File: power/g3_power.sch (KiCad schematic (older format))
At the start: 2 parts

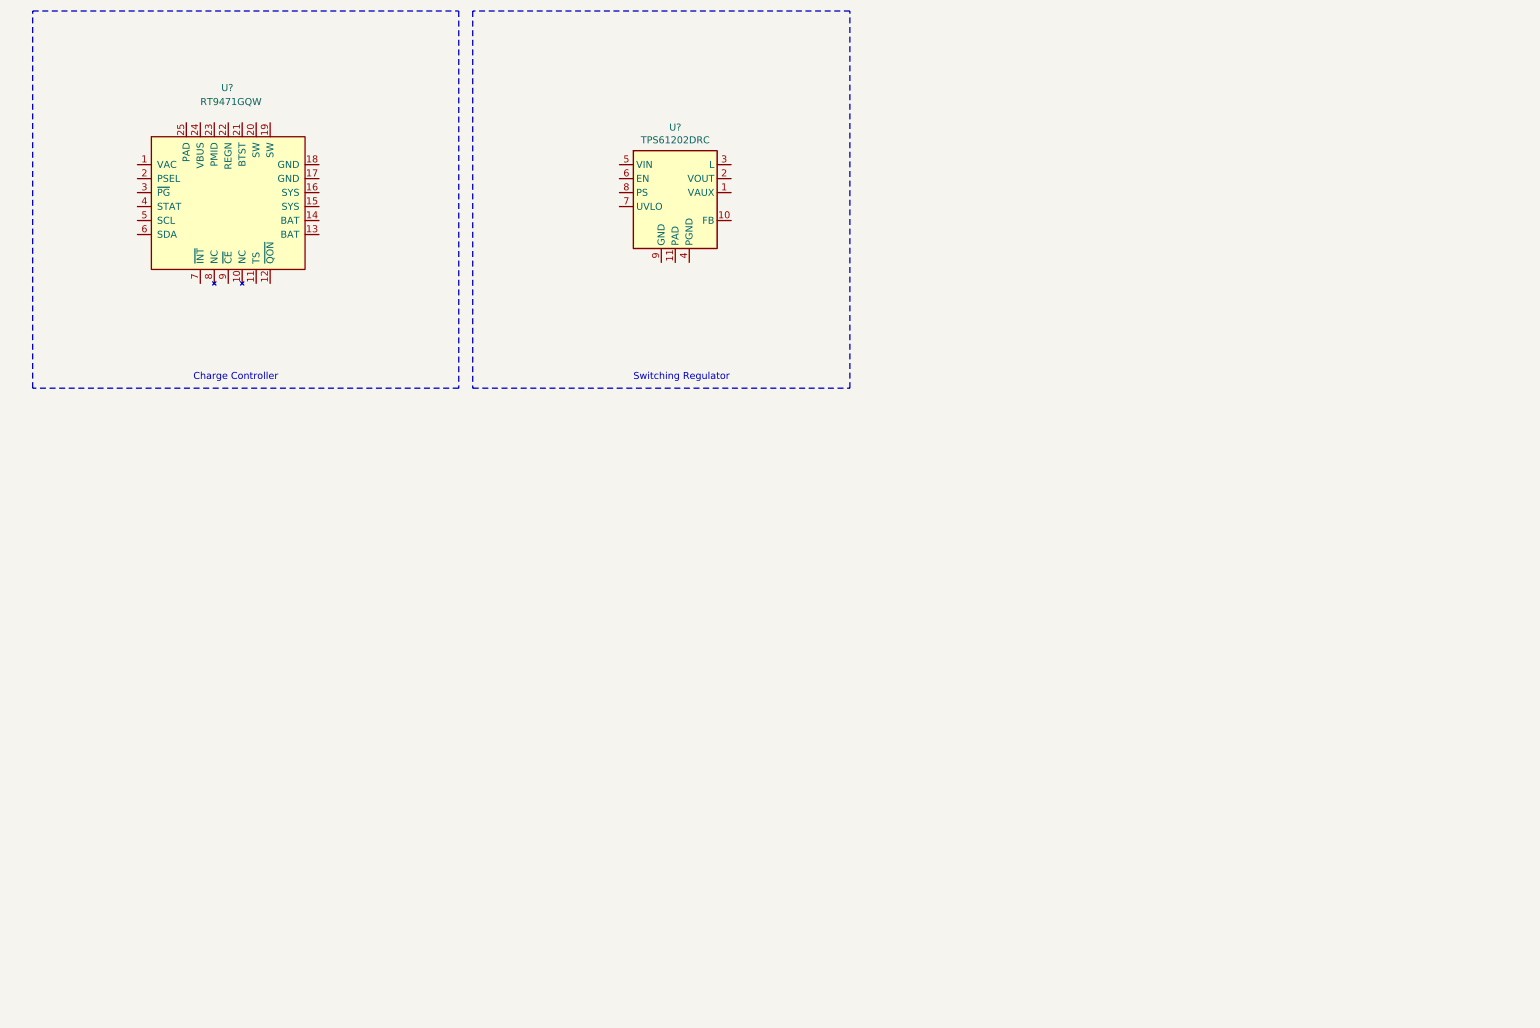
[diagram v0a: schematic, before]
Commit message: added interfacing to charge controller on schematic
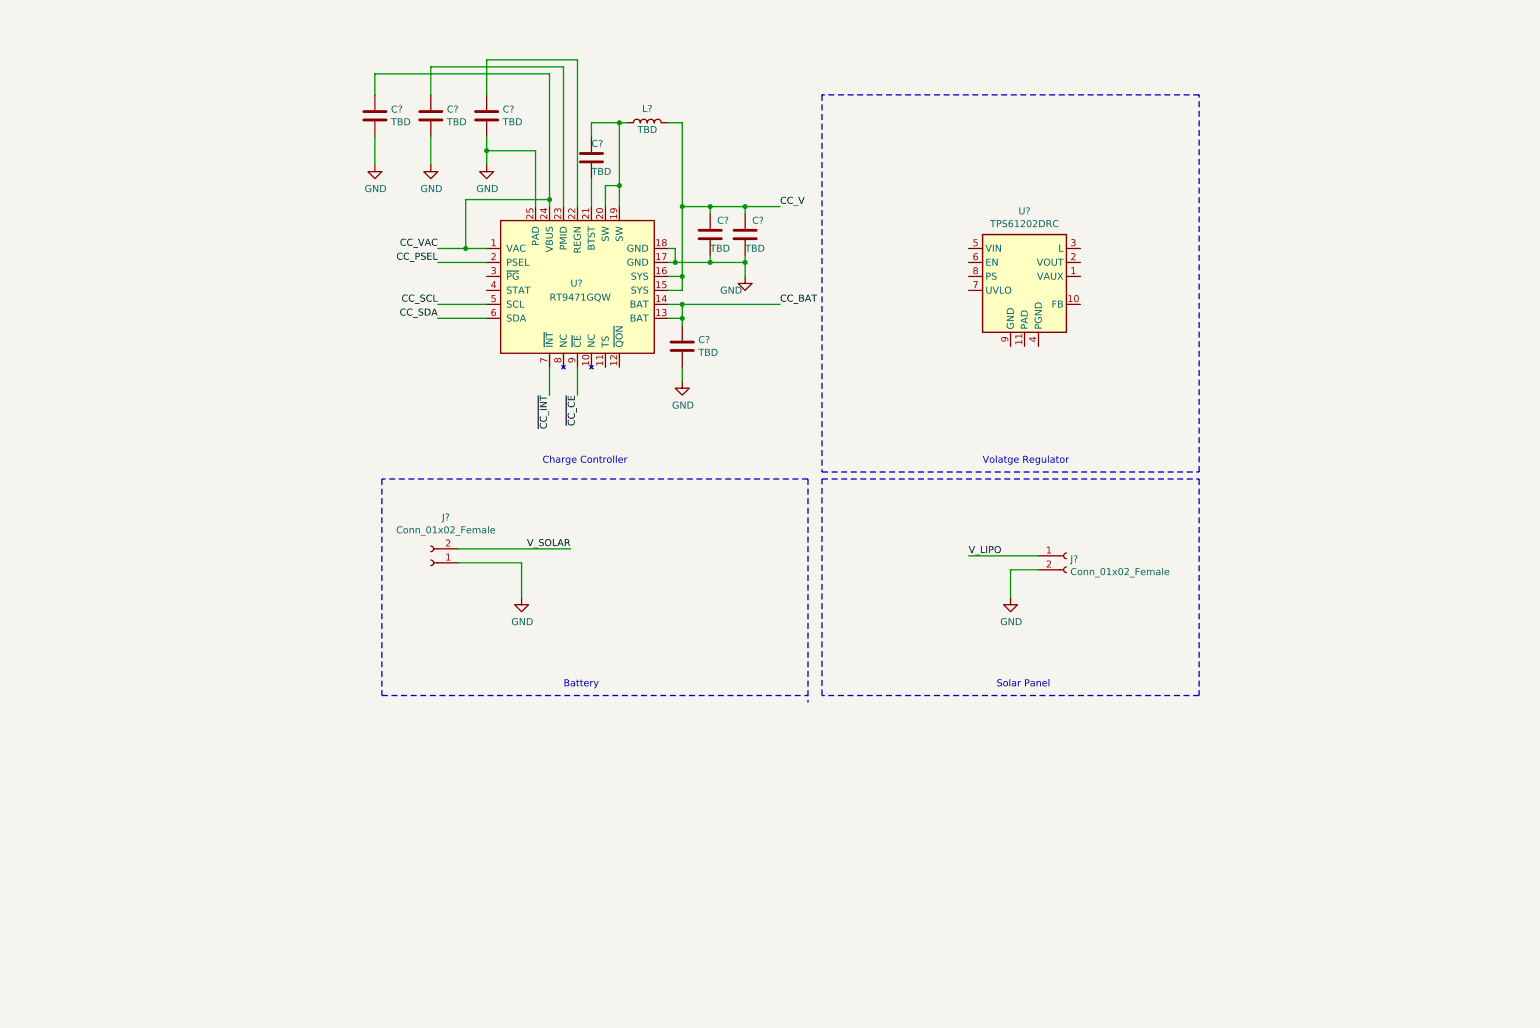
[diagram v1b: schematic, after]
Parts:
- added C? (x7): TBD, symbol Device:C
- added J? (x2): Conn_01x02_Female, symbol Connector:Conn_01x02_Female
- added L?: TBD, symbol Device:L
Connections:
- net CC_VAC: now reaches U?.1 (VAC)
- net CC_VAC: now also U?.24 (VBUS), C?.1
- net CC_BAT: now reaches U?.13 (BAT)
- net CC_BAT: now also U?.14 (BAT), C?.1
- net CC_V: now reaches U?.15 (SYS)
- net CC_V: now also U?.16 (SYS), C?.1, C?.1, L?.2
- net GND: now reaches U?.17 (GND)
- net GND: now also U?.18 (GND), U?.25 (PAD), C?.2, C?.2, C?.2, C?.2, C?.2, C?.2, J?.1 (Pin_1), J?.2 (Pin_2)
- net at U?.19 (SW): now also U?.20 (SW), C?.1, L?.1
- net CC_PSEL: now reaches U?.2 (PSEL)
- net at U?.21 (BTST): now also C?.2
- net at U?.22 (REGN): now also C?.1
- net at U?.23 (PMID): now also C?.1
- net CC_SCL: now reaches U?.5 (SCL)
- net CC_SDA: now reaches U?.6 (SDA)
- net ~CC_INT: now reaches U?.7 (~INT)
- net ~CC_CE: now reaches U?.9 (~CE)
- new net V_LIPO: J?.1 (Pin_1)
- new net V_SOLAR: J?.2 (Pin_2)
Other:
- note added: "Battery"
- note added: "Solar Panel"
- note added: "Volatge Regulator\n"
- note removed: "Switching Regulator\n"
- moved on the sheet: U?

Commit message: added VR interfacing on schematic
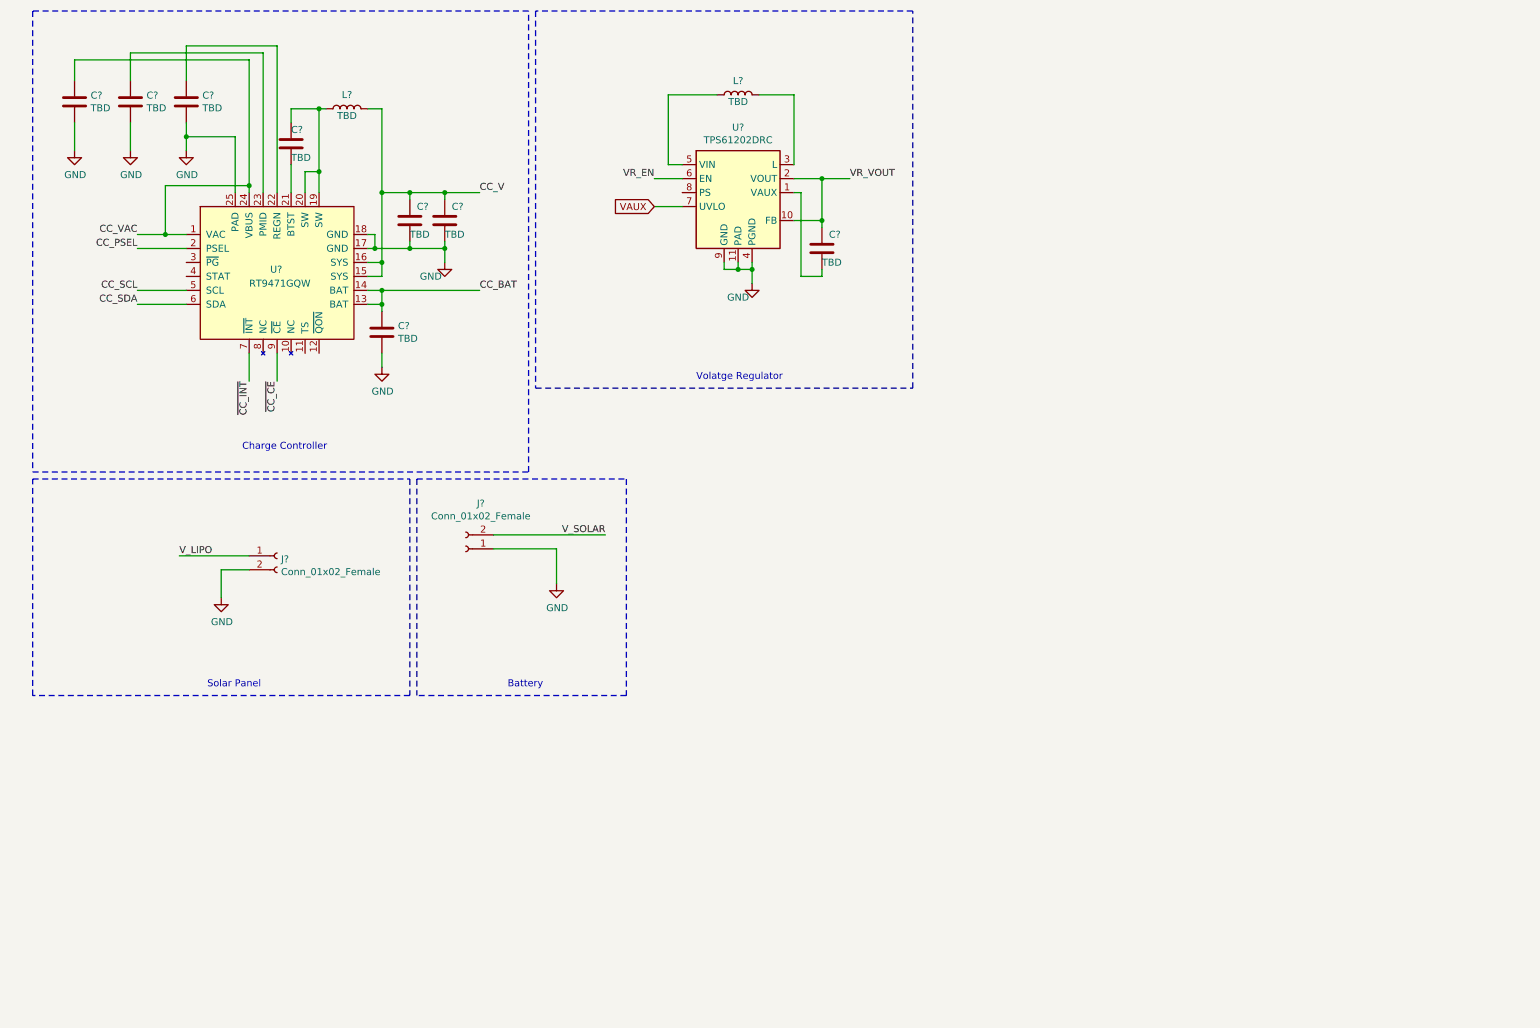
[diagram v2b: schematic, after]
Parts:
- added C?: TBD, symbol Device:C
- added L?: TBD, symbol Device:L
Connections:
- net GND: now also U?.11 (PAD), U?.4 (PGND), U?.9 (GND)
- net at U?.1 (VAUX): now also C?.2
- net VR_VOUT: now reaches U?.10 (FB)
- net VR_VOUT: now also U?.2 (VOUT), C?.1
- net at U?.3 (L): now also L?.2
- net at U?.5 (VIN): now also L?.1
- net VR_EN: now reaches U?.6 (EN)
- net VAUX: now reaches U?.7 (UVLO)
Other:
- moved on the sheet: C?, J?, L?, U?

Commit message: small changes to VR interfacing
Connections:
- net VR_PS: now reaches U?.8 (PS)
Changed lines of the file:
@@
 Wire Notes Line
 	550  3800 4100 3800
+Wire Wire Line
+	5200 1800 5000 1800
+Text Label 5000 1800 2    50   ~ 0
+VR_PS
 $EndSCHEMATC

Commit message: added fields for power BOM
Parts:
- C101: renamed from C?; value TBD -> 1uF
- C102, C105, C106, C107: renamed from C?; value TBD -> 10uF
- C103: renamed from C?; value TBD -> 4.7uF
- C104: renamed from C?; value TBD -> 47nF
- L101: renamed from L?; value TBD -> 1uH
- U101: renamed from U?; Description (none) -> Charge Controller; MFN (none) -> Richtek USA Inc.; MFP (none) -> RT9471GQW(2); S1PL (none) -> https://www.digikey.com/en/products/detail/richtek-usa-inc/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; S1PN (none) -> 1028-RT9471GQW(2)
- U102: renamed from U?; Description (none) -> Voltage Regulator; MFN (none) -> Texas Instruments; MFP (none) -> TPS61202DRCR; S1PL (none) -> https://www.digikey.com/en/products/detail/texas-instrument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; S1PN (none) -> 296-27462
- gave numbers to parts that had none: 4
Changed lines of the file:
@@
 $EndDescr
 $Comp
-L Connector:Conn_01x02_Female J?
+L Connector:Conn_01x02_Female J102
 U 1 1 61BA49C7
 P 3650 4350
-F 0 "J?" H 3542 4025 50  0000 C CNN
+F 0 "J102" H 3542 4025 50  0000 C CNN
 F 1 "Conn_01x02_Female" H 3542 4116 50  0000 C CNN
 F 2 "" H 3650 4350 50  0001 C CNN
@@
 $EndComp
 $Comp
-L Connector:Conn_01x02_Female J?
+L Connector:Conn_01x02_Female J101
 U 1 1 61BA5A31
 P 2300 4400
-F 0 "J?" H 2328 4376 50  0000 L CNN
+F 0 "J101" H 2328 4376 50  0000 L CNN
 F 1 "Conn_01x02_Female" H 2328 4285 50  0000 L CNN
 F 2 "" H 2300 4400 50  0001 C CNN
@@
 Solar Panel
 $Comp
-L power:GND #PWR?
+L power:GND #PWR0104
 U 1 1 61BA8023
 P 1900 4700
-F 0 "#PWR?" H 1900 4450 50  0001 C CNN
+F 0 "#PWR0104" H 1900 4450 50  0001 C CNN
 F 1 "GND" H 1905 4527 50  0000 C CNN
 F 2 "" H 1900 4700 50  0001 C CNN
@@
 V_LIPO
 $Comp
-L power:GND #PWR?
+L power:GND #PWR0107
 U 1 1 61BAA18A
 P 4300 4600
-F 0 "#PWR?" H 4300 4350 50  0001 C CNN
+F 0 "#PWR0107" H 4300 4350 50  0001 C CNN
 F 1 "GND" H 4305 4427 50  0000 C CNN
 F 2 "" H 4300 4600 50  0001 C CNN
@@
 	3250 1800 3250 1850
 $Comp
-L Device:C C?
+L Device:C C106
 U 1 1 61BE4E0B
 P 3250 2000
-F 0 "C?" H 3300 2100 50  0000 L CNN
-F 1 "TBD" H 3250 1900 50  0000 L CNN
+F 0 "C106" H 3300 2100 50  0000 L CNN
+F 1 "10uF" H 3250 1900 50  0000 L CNN
 F 2 "" H 3288 1850 50  0001 C CNN
 F 3 "~" H 3250 2000 50  0001 C CNN
@@
 	2950 2200 3000 2200
 $Comp
-L Device:C C?
+L Device:C C105
 U 1 1 61BD116E
 P 3050 2800
-F 0 "C?" H 3165 2846 50  0000 L CNN
-F 1 "TBD" H 3165 2755 50  0000 L CNN
+F 0 "C105" H 3165 2846 50  0000 L CNN
+F 1 "10uF" H 3165 2755 50  0000 L CNN
 F 2 "" H 3088 2650 50  0001 C CNN
 F 3 "~" H 3050 2800 50  0001 C CNN
@@
 	2600 1650 2600 1800
 $Comp
-L Device:C C?
+L Device:C C107
 U 1 1 61BC3A72
 P 3500 2000
-F 0 "C?" H 3550 2100 50  0000 L CNN
-F 1 "TBD" H 3500 1900 50  0000 L CNN
+F 0 "C107" H 3550 2100 50  0000 L CNN
+F 1 "10uF" H 3500 1900 50  0000 L CNN
 F 2 "" H 3538 1850 50  0001 C CNN
 F 3 "~" H 3500 2000 50  0001 C CNN
@@
 	1250 800  2200 800
 $Comp
-L power:GND #PWR?
+L power:GND #PWR0105
 U 1 1 61BBF70E
 P 3050 3050
-F 0 "#PWR?" H 3050 2800 50  0001 C CNN
+F 0 "#PWR0105" H 3050 2800 50  0001 C CNN
 F 1 "GND" H 3055 2877 50  0000 C CNN
 F 2 "" H 3050 3050 50  0001 C CNN
@@
 CC_V
 $Comp
-L Device:L L?
+L Device:L L101
 U 1 1 61BB7E31
 P 2800 1200
-F 0 "L?" V 2900 1200 50  0000 C CNN
-F 1 "TBD" V 2750 1200 50  0000 C CNN
+F 0 "L101" V 2900 1200 50  0000 C CNN
+F 1 "1uH" V 2750 1200 50  0000 C CNN
 F 2 "" H 2800 1200 50  0001 C CNN
 F 3 "~" H 2800 1200 50  0001 C CNN
@@
 	1650 1500 1650 1400
 $Comp
-L power:GND #PWR?
+L power:GND #PWR0103
 U 1 1 61BB4B72
 P 1650 1500
-F 0 "#PWR?" H 1650 1250 50  0001 C CNN
+F 0 "#PWR0103" H 1650 1250 50  0001 C CNN
 F 1 "GND" H 1655 1327 50  0000 C CNN
 F 2 "" H 1650 1500 50  0001 C CNN
@@
 $EndComp
 $Comp
-L Device:C C?
+L Device:C C103
 U 1 1 61BB43BB
 P 1650 1150
-F 0 "C?" H 1765 1196 50  0000 L CNN
-F 1 "TBD" H 1765 1105 50  0000 L CNN
+F 0 "C103" H 1765 1196 50  0000 L CNN
+F 1 "4.7uF" H 1765 1105 50  0000 L CNN
 F 2 "" H 1688 1000 50  0001 C CNN
 F 3 "~" H 1650 1150 50  0001 C CNN
@@
 $EndComp
 $Comp
-L Device:C C?
+L Device:C C104
 U 1 1 61BB0684
 P 2400 1450
-F 0 "C?" H 2400 1550 50  0000 L CNN
-F 1 "TBD" H 2400 1350 50  0000 L CNN
+F 0 "C104" H 2400 1550 50  0000 L CNN
+F 1 "47nF" H 2400 1350 50  0000 L CNN
 F 2 "" H 2438 1300 50  0001 C CNN
 F 3 "~" H 2400 1450 50  0001 C CNN
@@
 $EndComp
 $Comp
-L power:GND #PWR?
+L power:GND #PWR0102
 U 1 1 61BAFA76
 P 1250 1500
-F 0 "#PWR?" H 1250 1250 50  0001 C CNN
+F 0 "#PWR0102" H 1250 1250 50  0001 C CNN
 F 1 "GND" H 1255 1327 50  0000 C CNN
 F 2 "" H 1250 1500 50  0001 C CNN
@@
 $EndComp
 $Comp
-L Device:C C?
+L Device:C C102
 U 1 1 61BAF242
 P 1250 1150
-F 0 "C?" H 1365 1196 50  0000 L CNN
-F 1 "TBD" H 1365 1105 50  0000 L CNN
+F 0 "C102" H 1365 1196 50  0000 L CNN
+F 1 "10uF" H 1365 1105 50  0000 L CNN
 F 2 "" H 1288 1000 50  0001 C CNN
 F 3 "~" H 1250 1150 50  0001 C CNN
@@
 Charge Controller\n
 $Comp
-L RT9471GQW:RT9471GQW U?
+L RT9471GQW:RT9471GQW U101
 U 1 1 61BA69CD
 P 2300 2350
-F 0 "U?" H 2250 2350 50  0000 L CNN
+F 0 "U101" H 2250 2350 50  0000 L CNN
 F 1 "RT9471GQW" H 2100 2250 50  0000 L CNN
 F 2 "" H 2100 2850 50  0001 C CNN
-F 3 "" H 2100 2850 50  0001 C CNN
+F 3 "https://www.richtek.com/assets/product_file/RT9471=RT9471D/DS9471D-02.pdf" H 2100 2850 50  0001 C CNN
+F 4 "Charge Controller" H 2300 2350 50  0001 C CNN "Description"
+F 5 "Richtek USA Inc." H 2300 2350 50  0001 C CNN "MFN"
+F 6 "RT9471GQW(2)" H 2300 2350 50  0001 C CNN "MFP"
+F 7 "https://www.digikey.com/en/products/detail/richtek-usa-inc/RT9471GQW-2/13174421" H 2300 2350 50  0001 C CNN "S1PL"
+F 8 "1028-RT9471GQW(2)" H 2300 2350 50  0001 C CNN "S1PN"
+F 9 "" H 2300 2350 50  0001 C CNN "S2PL"
+F 10 "" H 2300 2350 50  0001 C CNN "S2PN"
 	1    2300 2350
 	1    0    0    -1
@@
 Connection ~ 2100 1750
 $Comp
-L Device:C C?
+L Device:C C101
 U 1 1 61C0041C
 P 850 1150
-F 0 "C?" H 965 1196 50  0000 L CNN
-F 1 "TBD" H 965 1105 50  0000 L CNN
+F 0 "C101" H 965 1196 50  0000 L CNN
+F 1 "1uF" H 965 1105 50  0000 L CNN
 F 2 "" H 888 1000 50  0001 C CNN
 F 3 "~" H 850 1150 50  0001 C CNN
@@
 $EndComp
 $Comp
-L power:GND #PWR?
+L power:GND #PWR0101
 U 1 1 61C00649
 P 850 1500
-F 0 "#PWR?" H 850 1250 50  0001 C CNN
+F 0 "#PWR0101" H 850 1250 50  0001 C CNN
 F 1 "GND" H 855 1327 50  0000 C CNN
 F 2 "" H 850 1500 50  0001 C CNN
@@
 	3050 2500 3750 2500
 $Comp
-L power:GND #PWR?
+L power:GND #PWR0106
 U 1 1 61C1BC81
 P 3500 2300
-F 0 "#PWR?" H 3500 2050 50  0001 C CNN
+F 0 "#PWR0106" H 3500 2050 50  0001 C CNN
 F 1 "GND" H 3400 2200 50  0000 C CNN
 F 2 "" H 3500 2300 50  0001 C CNN
@@
 	5700 2300 5700 2350
 $Comp
-L power:GND #PWR?
+L power:GND #PWR0108
 U 1 1 61C3620A
 P 5700 2450
-F 0 "#PWR?" H 5700 2200 50  0001 C CNN
+F 0 "#PWR0108" H 5700 2200 50  0001 C CNN
 F 1 "GND" H 5600 2350 50  0000 C CNN
 F 2 "" H 5700 2450 50  0001 C CNN
@@
 	6000 1800 6050 1800
 $Comp
-L Device:C C?
+L Device:C C108
 U 1 1 61C25B14
 P 6200 2200
-F 0 "C?" H 6250 2300 50  0000 L CNN
+F 0 "C108" H 6250 2300 50  0000 L CNN
 F 1 "TBD" H 6200 2100 50  0000 L CNN
 F 2 "" H 6238 2050 50  0001 C CNN
@@
 	6000 1600 6000 1100
 $Comp
-L Device:L L?
+L Device:L L102
 U 1 1 61C20B0F
 P 5600 1100
-F 0 "L?" V 5700 1100 50  0000 C CNN
+F 0 "L102" V 5700 1100 50  0000 C CNN
 F 1 "TBD" V 5550 1100 50  0000 C CNN
 F 2 "" H 5600 1100 50  0001 C CNN
@@
 $EndComp
 $Comp
-L Regulator_Switching:TPS61202DRC U?
+L Regulator_Switching:TPS61202DRC U102
 U 1 1 61BA5617
 P 5600 1800
-F 0 "U?" H 5600 2267 50  0000 C CNN
+F 0 "U102" H 5600 2267 50  0000 C CNN
 F 1 "TPS61202DRC" H 5600 2176 50  0000 C CNN
 F 2 "Package_SON:Texas_S-PVSON-N10_ThermalVias" H 5600 1350 50  0001 C CNN
 F 3 "http://www.ti.com/lit/ds/symlink/tps61200.pdf" H 5600 1800 50  0001 C CNN
+F 4 "Voltage Regulator" H 5600 1800 50  0001 C CNN "Description"
+F 5 "Texas Instruments" H 5600 1800 50  0001 C CNN "MFN"
+F 6 "TPS61202DRCR" H 5600 1800 50  0001 C CNN "MFP"
+F 7 "https://www.digikey.com/en/products/detail/texas-instruments/TPS61202DRCR/1908017" H 5600 1800 50  0001 C CNN "S1PL"
+F 8 "296-27462" H 5600 1800 50  0001 C CNN "S1PN"
 	1    5600 1800
 	1    0    0    -1
